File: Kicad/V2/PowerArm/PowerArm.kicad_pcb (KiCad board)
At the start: 2 copper layers, 113.8 x 113.8 mm, 73 parts, among them J1 JST_Connector_To_Wrist_Board, J2 USB Connector to Computer, J3 JST_Connector_To_Other_Glove, J4 XLR5_Ground, J5 USB Connector to Powerbank, U1 CH340K, U3 AMS1117, U4 74HC4052, U5 B0505S-1W1, U6 6N137, U7 MAX485E, U8 ATMEGA2561-16AU, Y2 16MHz

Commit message: route power block
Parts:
- J2, J5: footprint MyGlove:USB_C_Receptacle_GCT_USB4105-xx-A_16P_TopMnt_Horizontal -> MyGlove:USB_Conn
- moved C19 262.2 mm to (455.2, 63.8)
- moved C20 262.2 mm to (411.2, 70.5)
- moved C21 262.2 mm to (411.2, 73.0)
- moved C23 262.2 mm to (411.2, 75.5)
- moved C24 262.2 mm to (411.2, 78.0)
- moved C29 262.2 mm to (429.8, 77.7)
- moved C30 262.2 mm to (429.8, 80.2)
- moved R27 262.2 mm to (411.2, 65.6)
- moved R28 262.2 mm to (411.2, 68.0)
- moved U5 262.2 mm to (423.9, 64.8)
- moved U6 262.2 mm to (442.6, 65.3)
- moved U7 262.2 mm to (401.5, 71.2)
- moved C22 262.2 mm to (465.5, 59.1)
- moved J4 262.2 mm to (385.5, 70.2)
- moved D7 51.2 mm to (125.1, 27.8), turned to 180 degrees
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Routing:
- net Net-(J5-SHIELD): track 0.00 -> 22.7 mm
- net VCC: track 0.00 -> 12.3 mm
- net Net-(J5-CC2): track 0.00 -> 12.2 mm, vias 0 -> 2
- net GND: track 0.00 -> 11.2 mm, vias 0 -> 5
- net VBUS: track 0.00 -> 9.49 mm
- net Net-(J5-CC1): track 0.00 -> 9.43 mm, vias 0 -> 2
- net +3.3V: track 0.00 -> 7.67 mm
- net VCCL: track 0.00 -> 4.25 mm
- net Net-(D7-K): track 0.00 -> 2.05 mm
- added copper zone on F.Cu, net +3.3V
- added copper zone on F.Cu, net VBUS
- added copper zone on F.Cu, net VCC
- added copper zone on F.Cu, net VCCL
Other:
- board text added: "POWER"

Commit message: route ATmega capa and quarz
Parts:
- moved C29 277.4 mm to (153.8, 50.6), turned to 135 degrees
- moved C30 257.4 mm to (175.4, 41.5), turned to -45 degrees
- moved C14 83.2 mm to (55.4, 41.4), turned to 90 degrees
- moved U3 75.4 mm to (59.6, 48.7), turned to -90 degrees
- moved C13 74.8 mm to (59.6, 41.5), turned to 90 degrees
- moved C12 66.1 mm to (64.9, 51.8), turned to 0 degrees
- moved C25 31.0 mm to (177.0, 37.2)
- moved C26 31.0 mm to (172.0, 32.6)
- moved Y2 31.0 mm to (174.6, 34.9)
- moved U8 28.4 mm to (165.1, 46.0)
- moved R29 28.4 mm to (175.9, 56.9)
- moved C31 27.4 mm to (161.7, 58.3), turned to -135 degrees
- moved C11 14.9 mm to (125.4, 39.7), turned to 180 degrees
- moved FB01 0.80 mm to (129.7, 32.7)
- moved R15 0.80 mm to (116.2, 39.2)
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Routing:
- net /ATMega2561/2561_SDA: track 55.3 -> 21.3 mm
- net /ATMega2561/2561_SCL: track 55.2 -> 21.4 mm
- net /ATMega2561/2561_RXD1: track 57.3 -> 23.5 mm
- net /ATMega2561/2561_TXD1: track 58.6 -> 24.9 mm
- net /ATMega2561/MCU_2561_RESET: track 0.00 -> 18.9 mm
- net /ATMega2561/2561_TOUCH_INT: track 40.3 -> 32.1 mm
- net VCC: track 12.3 -> 18.7 mm
- net +3.3V: track 7.67 -> 13.6 mm
- net Net-(U8-XTAL1): track 8.47 -> 12.0 mm
- net GND: track 11.2 -> 14.4 mm, vias 5 -> 9
- net Net-(U8-XTAL2): track 11.6 -> 13.3 mm
- removed copper zone on F.Cu, net VCC

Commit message: route UART
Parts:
- removed C12, C14: 100nF, MyGlove:Capacitor_0603
- removed C13: 10uF, MyGlove:Capacitor_0603
- removed U3: AMS1117, MyGlove:AMS1117
- J1: footprint MyGlove:FPC_CONNECTOR_24 -> MyGlove:conn_zif_20x0.5mm
- moved TP1 247.3 mm to (252.2, 144.3)
- moved TP17 247.3 mm to (252.2, 150.4)
- moved TP18 247.3 mm to (252.2, 153.4)
- moved TP19 247.3 mm to (252.2, 156.5)
- moved TP2 247.3 mm to (252.2, 147.3)
- moved TP20 247.3 mm to (255.2, 144.3)
- moved TP21 247.3 mm to (255.2, 147.3)
- moved TP22 247.3 mm to (255.2, 150.4)
- moved TP23 247.3 mm to (255.2, 153.4)
- moved TP24 247.3 mm to (255.2, 156.5)
- moved TP25 247.3 mm to (258.3, 144.3)
- moved TP26 247.3 mm to (258.3, 147.3)
- moved TP27 247.3 mm to (258.3, 150.4)
- moved C27 81.4 mm to (194.8, 85.9)
- moved C28 81.4 mm to (189.8, 84.3)
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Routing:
- net /ATMega2561/MOSI_BOOT_2561: track 0.00 -> 62.0 mm
- net /ATMega2561/MISO_BOOT_2561: track 0.00 -> 60.5 mm
- net /ATMega2561/2561_SDA: track 21.3 -> 51.3 mm, vias 0 -> 2
- net /ATMega2561/2561_RXD1: track 23.5 -> 52.4 mm
- net /ATMega2561/2561_SCL: track 21.4 -> 49.3 mm, vias 0 -> 2
- net /ATMega2561/2561_TXD1: track 24.9 -> 51.7 mm, vias 2 -> 0
- net Net-(J2-SHIELD): track 0.00 -> 22.6 mm
- net /ATMega2561/2561_TOUCH_INT: track 32.1 -> 11.3 mm
- net GND: track 14.4 -> 33.8 mm, vias 9 -> 22
- net /ATMega2561/MCU_2561_RESET: track 18.9 -> 0.00 mm
- net Net-(D9-K): track 0.00 -> 17.8 mm
- net Net-(U1-RXD): track 0.00 -> 16.4 mm
- net Net-(J3-Rx): track 0.00 -> 16.3 mm
- net +3.3V: track 13.6 -> 0.00 mm
- net /ATMega2561/2561_TOUCH_RESET: track 0.00 -> 13.4 mm
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- removed copper zone on F.Cu, net +3.3V
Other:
- board size 113.8 x 113.8 mm -> 113.8 x 78.9 mm
- board text added: "Rx"
- board text added: "Tx"
- board text added: "UART"

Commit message: route DMX
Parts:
- moved C22 328.0 mm to (138.2, 79.5), turned to 90 degrees
- moved C19 298.3 mm to (157.4, 80.7), turned to -90 degrees
- moved U6 288.9 mm to (155.1, 93.2)
- moved U5 276.4 mm to (147.9, 79.5), turned to 180 degrees
- moved C23 275.0 mm to (137.0, 96.8)
- moved C24 274.6 mm to (137.0, 93.4)
- moved R27 266.7 mm to (146.5, 98.8)
- moved R28 265.9 mm to (145.9, 86.8), turned to -90 degrees
- moved C21 265.9 mm to (145.3, 77.3), turned to 180 degrees
- moved U7 261.9 mm to (140.1, 88.2)
- moved J4 261.2 mm to (125.0, 88.9)
- moved C20 259.5 mm to (151.8, 76.5), turned to 90 degrees
- moved TP6 154.3 mm to (154.2, 27.6)
- moved TP2 151.7 mm to (139.8, 45.5)
- moved TP13 148.1 mm to (155.6, 43.6)
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- renumbered TP24 to TP10, TP25 to TP11, TP26 to TP12, TP27 to TP13, TP17 to TP3, TP18 to TP4, TP19 to TP5, TP20 to TP6, TP21 to TP7, TP22 to TP8, TP23 to TP9
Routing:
- net VCC: track 11.2 -> 201.9 mm, vias 0 -> 11
- net Net-(J4-P1): track 0.00 -> 82.0 mm
- net /ATMega2561/DTR: track 13.2 -> 91.3 mm, vias 2 -> 4
- net /Data/DMX/TX_DMX: track 0.00 -> 61.8 mm
- net VCCL: track 4.25 -> 65.1 mm, vias 0 -> 2
- net /ATMega2561/MCU_2561_RESET: track 0.00 -> 58.8 mm, vias 0 -> 4
- net Net-(U5-+VO): track 0.00 -> 53.4 mm, vias 0 -> 4
- net /ATMega2561/2561_MUX_SELECT_B: track 2.06 -> 38.3 mm, vias 1 -> 2
- net /ATMega2561/2561_MUX_SELECT_A: track 2.09 -> 37.9 mm, vias 1 -> 2
- net /ATMega2561/SCK_BOOT_2561: track 11.3 -> 46.3 mm, vias 0 -> 2
- net /ATMega2561/2561_USB1_INT: track 0.00 -> 28.1 mm, vias 0 -> 2
- net VBUS: track 9.49 -> 31.7 mm, vias 0 -> 2
- net /ATMega2561/2561_RXD1: track 52.4 -> 35.7 mm
- net GND: track 33.8 -> 50.4 mm, vias 22 -> 31
- net /ATMega2561/MISO_BOOT_2561: track 60.5 -> 44.4 mm
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- added copper zone on B.Cu, net GND
- added copper zone on F.Cu, net VCC
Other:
- board size 113.8 x 78.9 mm -> 60.1 x 79.1 mm
- board text added: "ATMega2561"
- board text added: "BOOT"
- board text added: "DMX"
- board text added: "G-Love V2.0 - PowerArm Board"
- board text added: "WRIST"

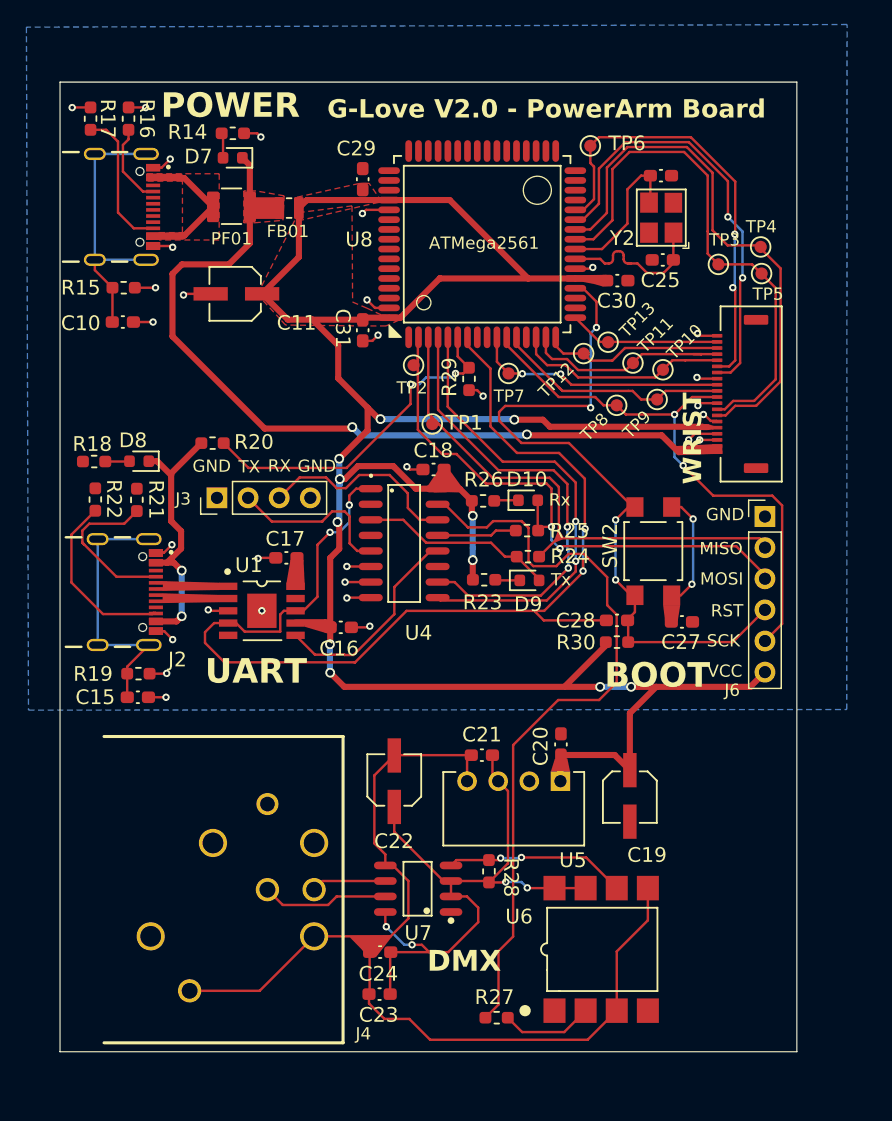
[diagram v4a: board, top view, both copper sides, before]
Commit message: route gnd planes
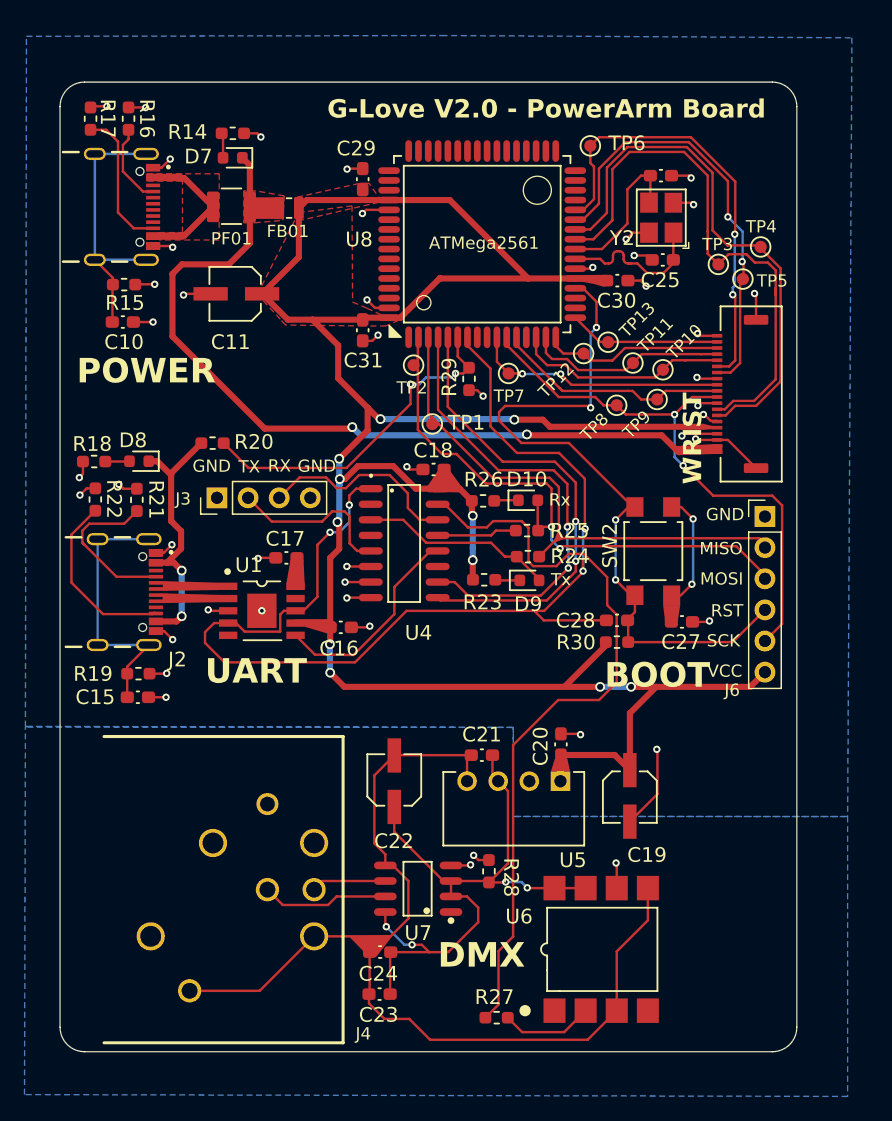
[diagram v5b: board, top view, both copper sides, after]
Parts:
- moved TP5 1.59 mm to (166.6, 38.5)
- moved R15 0.26 mm to (116.1, 38.9)
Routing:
- net GND: track 50.4 -> 81.8 mm, vias 31 -> 44
- net Net-(U6-VO): track 14.8 -> 5.10 mm, vias 2 -> 3
- net /ATMega2561/2561_SCL: track 43.3 -> 45.4 mm
- net /ATMega2561/2561_SCREEN_RESET: track 17.0 -> 16.4 mm
- added copper zone on B.Cu, net Net-(U6-VO)
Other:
- outline, holes or cut-outs redrawn

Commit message: start stitching
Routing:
- net Net-(J4-P1): track 82.0 -> 0.00 mm
- net Net-(U6-VO): track 5.10 -> 18.2 mm, vias 3 -> 2
- net GND: track 81.8 -> 77.0 mm, vias 44 -> 57
- net VCC: track 201.5 -> 206.2 mm
- added copper zone on F.Cu, net GND
- added copper zone on B.Cu, net Net-(J4-P1)
- added copper zone on F.Cu, net Net-(J4-P1)
- removed copper zone on B.Cu, net Net-(U6-VO)

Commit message: minor fixes on powerboard
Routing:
- net GND: track 77.0 -> 60.3 mm, vias 57 -> 77
- net /ATMega2561/2561_SCL: track 45.4 -> 44.0 mm
- net VCC: track 206.2 -> 205.7 mm, vias 11 -> 13

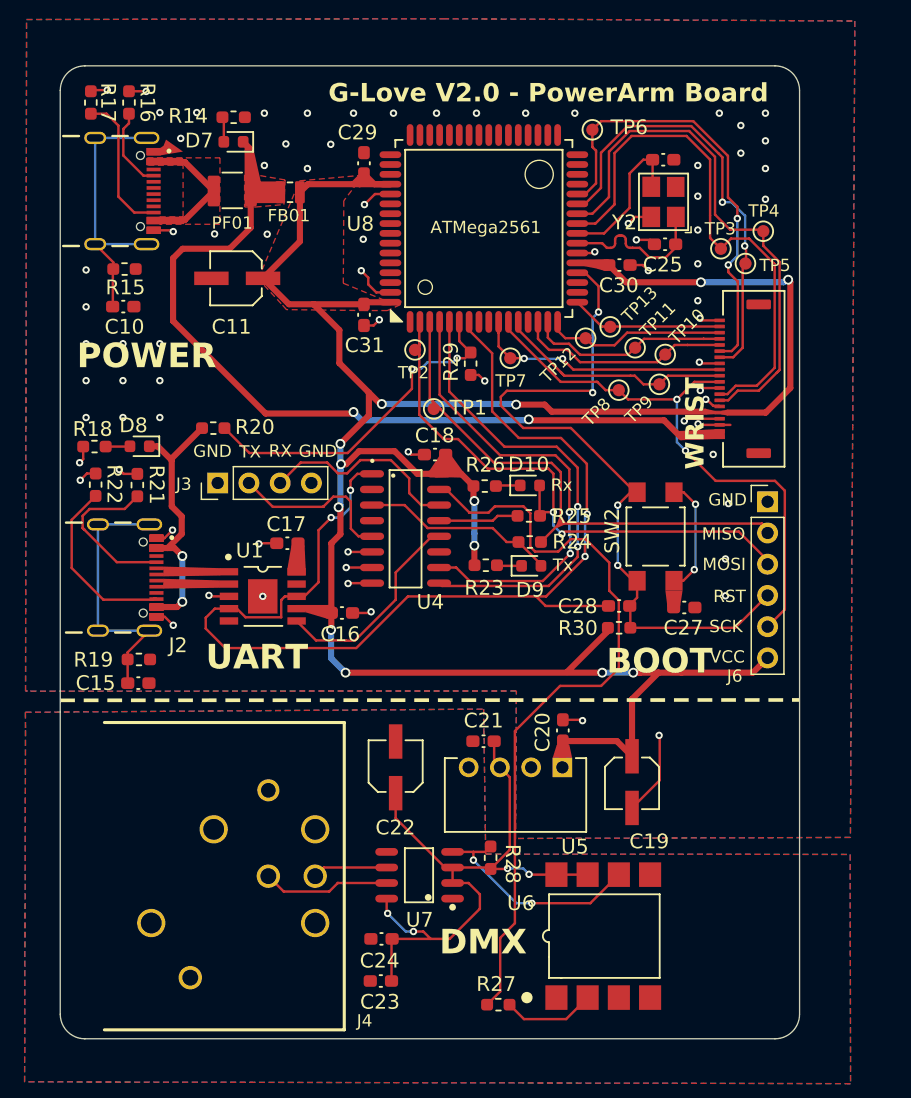
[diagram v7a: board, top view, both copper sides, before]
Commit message: touchup on stitching and usb connector footprint
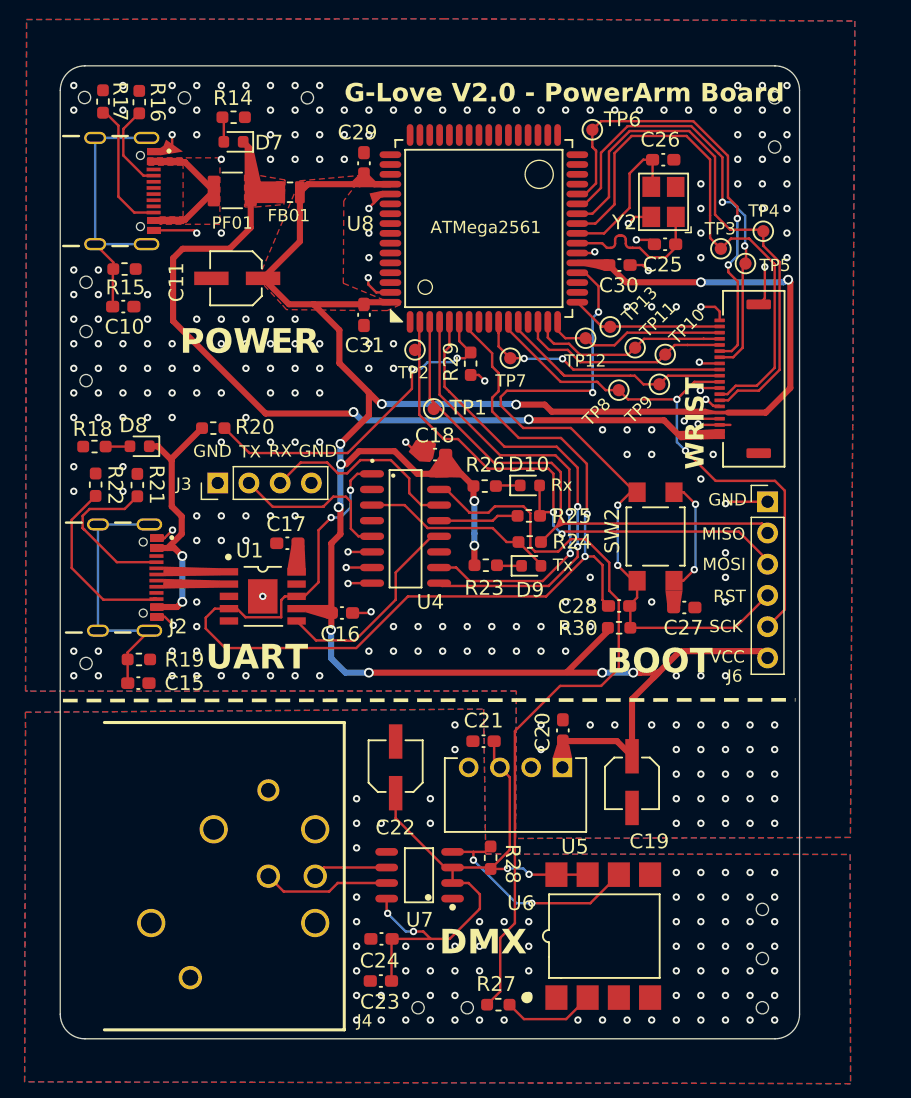
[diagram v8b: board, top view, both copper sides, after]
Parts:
- added G***: LOGO, MyGlove:logoSilk, F.Cu at (145.3, 35.6)
- added REF**: NPTH_Drill_Hole, MyGlove:NPTH_Drill_Hole, F.Cu at (121.0, 25.0)
- added REF**: NPTH_Drill_Hole, MyGlove:NPTH_Drill_Hole, F.Cu at (113.0, 48.0)
- added REF**: NPTH_Drill_Hole, MyGlove:NPTH_Drill_Hole, F.Cu at (113.0, 44.0)
- added REF**: NPTH_Drill_Hole, MyGlove:NPTH_Drill_Hole, F.Cu at (113.0, 71.0)
- added REF**: NPTH_Drill_Hole, MyGlove:NPTH_Drill_Hole, F.Cu at (168.0, 99.0)
- added REF**: NPTH_Drill_Hole, MyGlove:NPTH_Drill_Hole, F.Cu at (168.0, 95.0)
- added REF**: NPTH_Drill_Hole, MyGlove:NPTH_Drill_Hole, F.Cu at (169.0, 25.0)
- added REF**: NPTH_Drill_Hole, MyGlove:NPTH_Drill_Hole, F.Cu at (144.0, 99.0)
- added REF**: NPTH_Drill_Hole, MyGlove:NPTH_Drill_Hole, F.Cu at (112.9, 25.0)
- added REF**: NPTH_Drill_Hole, MyGlove:NPTH_Drill_Hole, F.Cu at (168.0, 91.0)
- added REF**: NPTH_Drill_Hole, MyGlove:NPTH_Drill_Hole, F.Cu at (140.0, 99.0)
- added REF**: NPTH_Drill_Hole, MyGlove:NPTH_Drill_Hole, F.Cu at (113.0, 40.0)
- added REF**: NPTH_Drill_Hole, MyGlove:NPTH_Drill_Hole, F.Cu at (131.0, 25.0)
- added REF**: NPTH_Drill_Hole, MyGlove:NPTH_Drill_Hole, F.Cu at (169.0, 29.0)
- moved R17 0.99 mm to (114.4, 25.3)
- moved R16 0.84 mm to (117.3, 25.4)
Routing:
- net GND: track 60.3 -> 49.9 mm, vias 77 -> 246
- net /ATMega2561/DTR: track 91.2 -> 89.8 mm
- net VCC: track 205.7 -> 206.7 mm
- net Net-(J5-CC2): track 11.8 -> 10.9 mm
- net Net-(J4-P1): vias 0 -> 77
